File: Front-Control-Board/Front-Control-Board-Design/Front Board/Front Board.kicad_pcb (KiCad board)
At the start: 2 copper layers, 78 x 53.5 mm, 25 parts, among them J1 Conn_01x08, J2 Conn_01x23, Q1 2N7002, U1 MAX33054EASA+T, U2 TS2940CP33 ROG, U3 ESP32-DevKitC

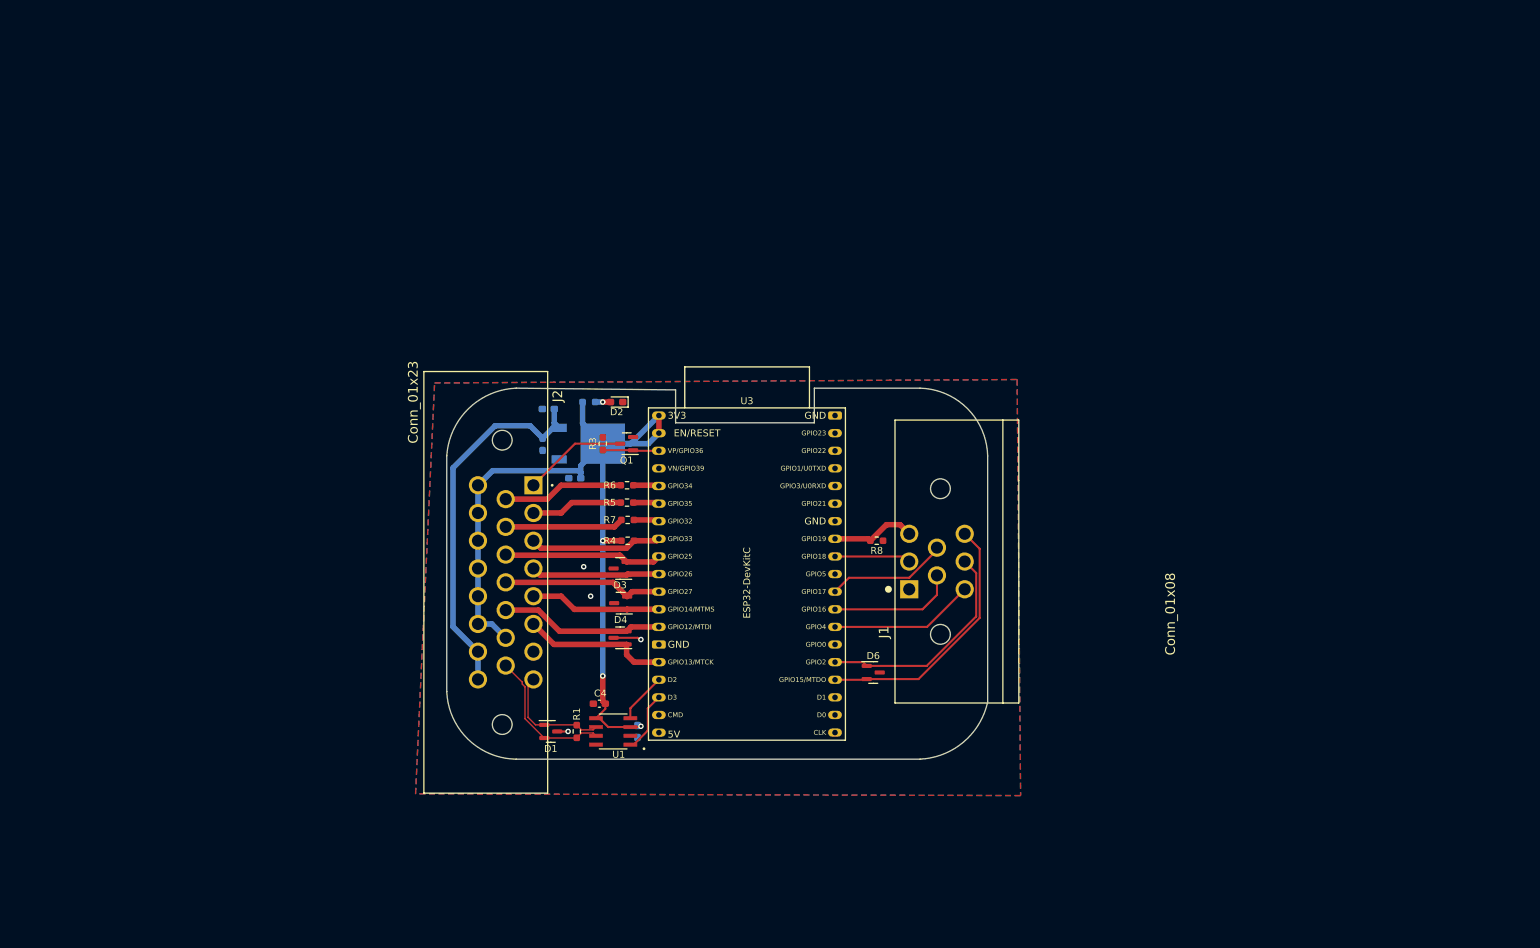
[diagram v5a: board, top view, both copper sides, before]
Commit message: pin layout updated needs PCB
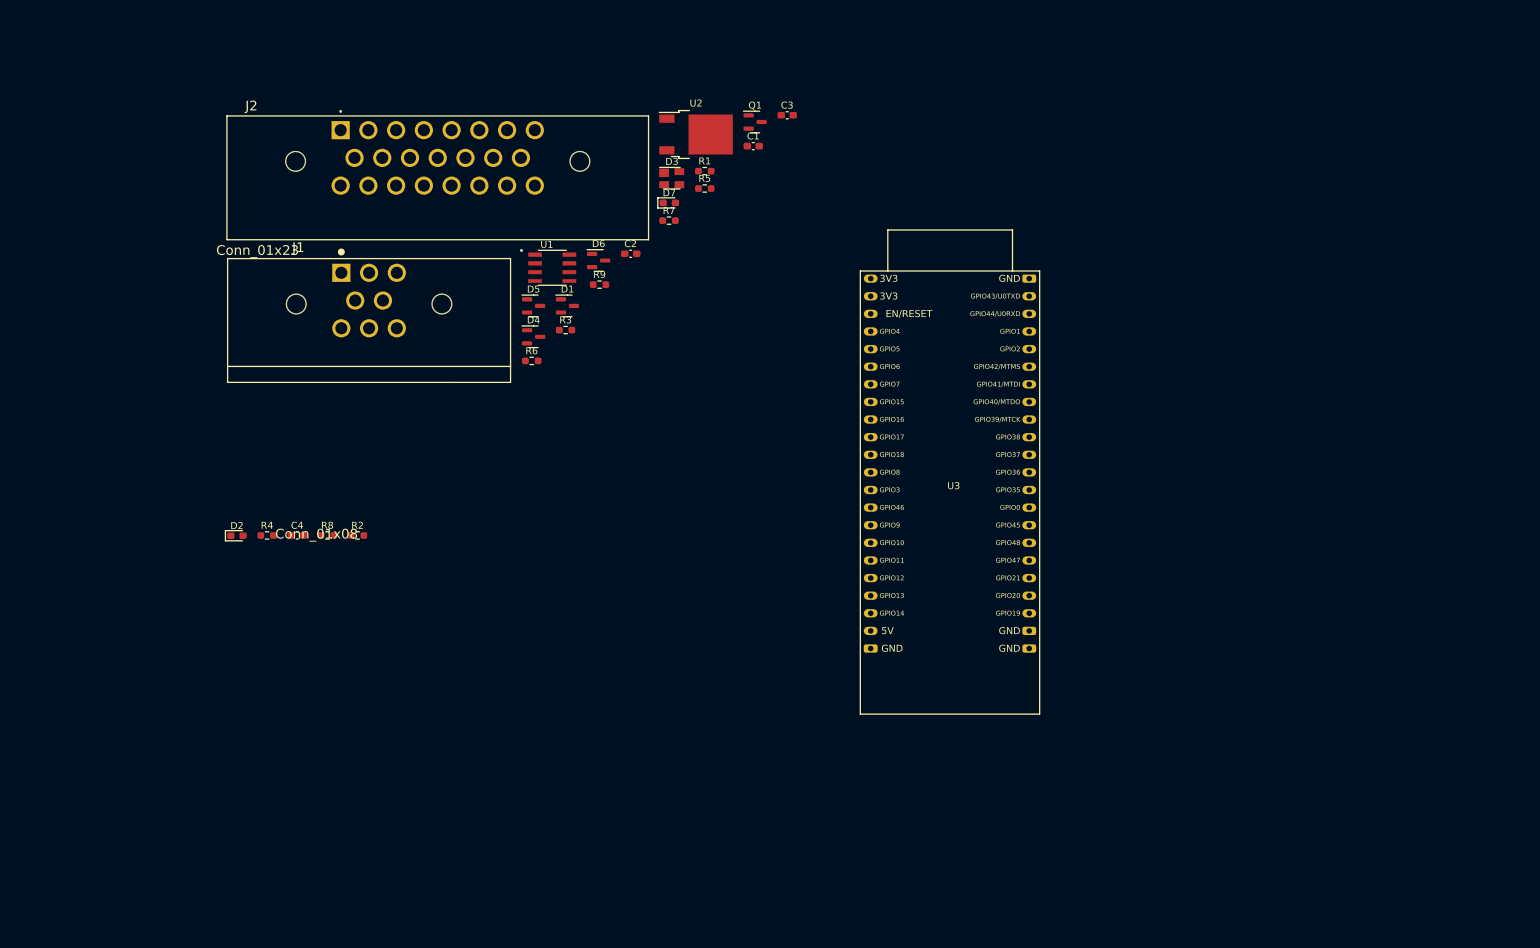
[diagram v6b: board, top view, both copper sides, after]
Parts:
- added R9: 100, Resistor_SMD:R_0603_1608Metric_Pad0.98x0.95mm_HandSolder, F.Cu at (132.0, 77.1)
- C1, C2, C3, D7, R2, U2: moved to F.Cu
- D3: value SP0502BAHT -> SP0503BAHT; footprint Package_TO_SOT_SMD:SOT-23 -> Package_TO_SOT_SMD:SOT-143
- R4: value 10k -> 100
- R7: value 100 -> 10k
- U3: footprint Espressif:ESP32-DevKitC -> AERO_Footprints:ESP32-DEV C
- moved C3 91.4 mm to (159.1, 52.6), turned to 0 degrees
- moved J1 90.4 mm to (98.8, 79.9), turned to 0 degrees
- moved R1 82.9 mm to (147.2, 60.7), turned to 0 degrees
- moved R8 79.2 mm to (92.8, 113.2), turned to 0 degrees
- moved D6 71.4 mm to (131.9, 73.6)
- moved U1 67.4 mm to (125.2, 74.6), turned to 0 degrees
- moved D1 61.4 mm to (127.4, 80.1)
- moved J2 58.3 mm to (94.7, 54.8), turned to 0 degrees
- moved D2 58.1 mm to (79.7, 113.3), turned to 0 degrees
- moved D3 56.8 mm to (142.4, 61.7), turned to 0 degrees
- moved R4 52.0 mm to (84.1, 113.2), turned to 0 degrees
- moved Q1 49.9 mm to (154.5, 53.6), turned to 0 degrees
- moved C4 49.9 mm to (88.4, 113.2), turned to 0 degrees
- moved D5 49.5 mm to (122.5, 80.1), turned to 0 degrees
- moved C1 48.1 mm to (154.2, 57.1), turned to 0 degrees
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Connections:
- D3 pad 1: /pedal_1 -> unconnected-(D3-Pad1)
- D3 pad 2: /stearing -> /R_wheel
- D3 pad 3: GND -> /L_wheel
- D4 pad 1: /R_wheel -> /R_sus
- D4 pad 2: /L_wheel -> /stearing
- D5 pad 1: /R_sus -> /pedal_0
- D5 pad 2: /L_sus -> /pedal_1
- D6 pad 1: /Brake_0 -> /Brake_1
- D6 pad 2: /Brake_1 -> /Brake_0
- R4 pad 1: /RTD_bttn -> Net-(U3-Pad35)
- R4 pad 2: VDD -> /AMS_Led
- R5 pad 1: Net-(R5-Pad1) -> /IMD_led
- R5 pad 2: /IMD_led -> Net-(U3-Pad34)
- R6 pad 1: Net-(R6-Pad1) -> Net-(U3-Pad33)
- R6 pad 2: /AMS_Led -> /RTD_led
- R7 pad 1: Net-(R7-Pad1) -> /RTD_bttn
- R7 pad 2: /RTD_led -> GND
- U1 pad 1: /CAN_TX -> /CAN_MOSI
- U1 pad 4: /CAN_RX -> /CAN_MISO
- U3 pad 10: /pedal_1 -> Net-(U3-Pad10)
- U3 pad 11: /L_wheel -> unconnected-(U3-Pad11)
- U3 pad 12: /R_wheel -> /LORA_SCK
- U3 pad 13: /L_sus -> /LORA_MISO
- U3 pad 15: /R_sus -> /Laura_MOSI
- U3 pad 16: /CAN_RX -> unconnected-(U3-Pad16)
- U3 pad 17: /CAN_TX -> unconnected-(U3-Pad17)
- U3 pad 23: /Brake_1 -> /LoRa_CS
- U3 pad 24: /Brake_0 -> unconnected-(U3-Pad24)
- U3 pad 25: unconnected-(U3-Pad25) -> /Brake_1
- U3 pad 26: /pedal_0 -> /Brake_0
- U3 pad 27: /LORA_RX -> /RTD_ind_sig
- U3 pad 28: /LORA_TX -> /RTD_bttn
- U3 pad 29: unconnected-(U3-Pad29) -> /CAN_CS
- U3 pad 3: /RTD_ind_sig -> /R_wheel
- U3 pad 30: /LORA NSS -> /CAN_SCK
- U3 pad 31: /LORA Reset -> /CAN_MISO
- U3 pad 33: unconnected-(U3-Pad33) -> Net-(U3-Pad33)
- U3 pad 34: unconnected-(U3-Pad34) -> Net-(U3-Pad34)
- U3 pad 35: unconnected-(U3-Pad35) -> Net-(U3-Pad35)
- U3 pad 36: unconnected-(U3-Pad36) -> /LORA Reset
- U3 pad 37: unconnected-(U3-Pad37) -> /CAN_MOSI
- U3 pad 4: unconnected-(U3-Pad4) -> /L_wheel
- U3 pad 5: Net-(R6-Pad1) -> /L_sus
- U3 pad 6: Net-(R5-Pad1) -> /R_sus
- U3 pad 7: Net-(R7-Pad1) -> /stearing
- U3 pad 8: /RTD_bttn -> /pedal_0
- U3 pad 9: /stearing -> /pedal_1
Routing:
- net VDD: track 125.7 -> 0.00 mm, vias 3 -> 0
- net +12V: track 54.2 -> 0.00 mm
- net /Brake_1: track 37.6 -> 0.00 mm
- net /Brake_0: track 32.1 -> 0.00 mm
- net /L_sus: track 23.6 -> 0.00 mm
- net /L_wheel: track 23.2 -> 0.00 mm
- net /stearing: track 22.8 -> 0.00 mm
- net /R_sus: track 21.2 -> 0.00 mm
- net /pedal_0: track 20.9 -> 0.00 mm
- net /CAN_P: track 20.7 -> 0.00 mm
- net /RTD_bttn: track 19.5 -> 0.00 mm
- net /R_wheel: track 18.9 -> 0.00 mm
- net /pedal_1: track 18.5 -> 0.00 mm
- net /LORA_RX: track 18.4 -> 0.00 mm
- net /LORA_TX: track 17.5 -> 0.00 mm
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- removed copper zone on B.Cu, net GND
- removed copper zone on F.Cu, net GND
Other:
- board outline removed

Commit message: Front board updated just needs traces
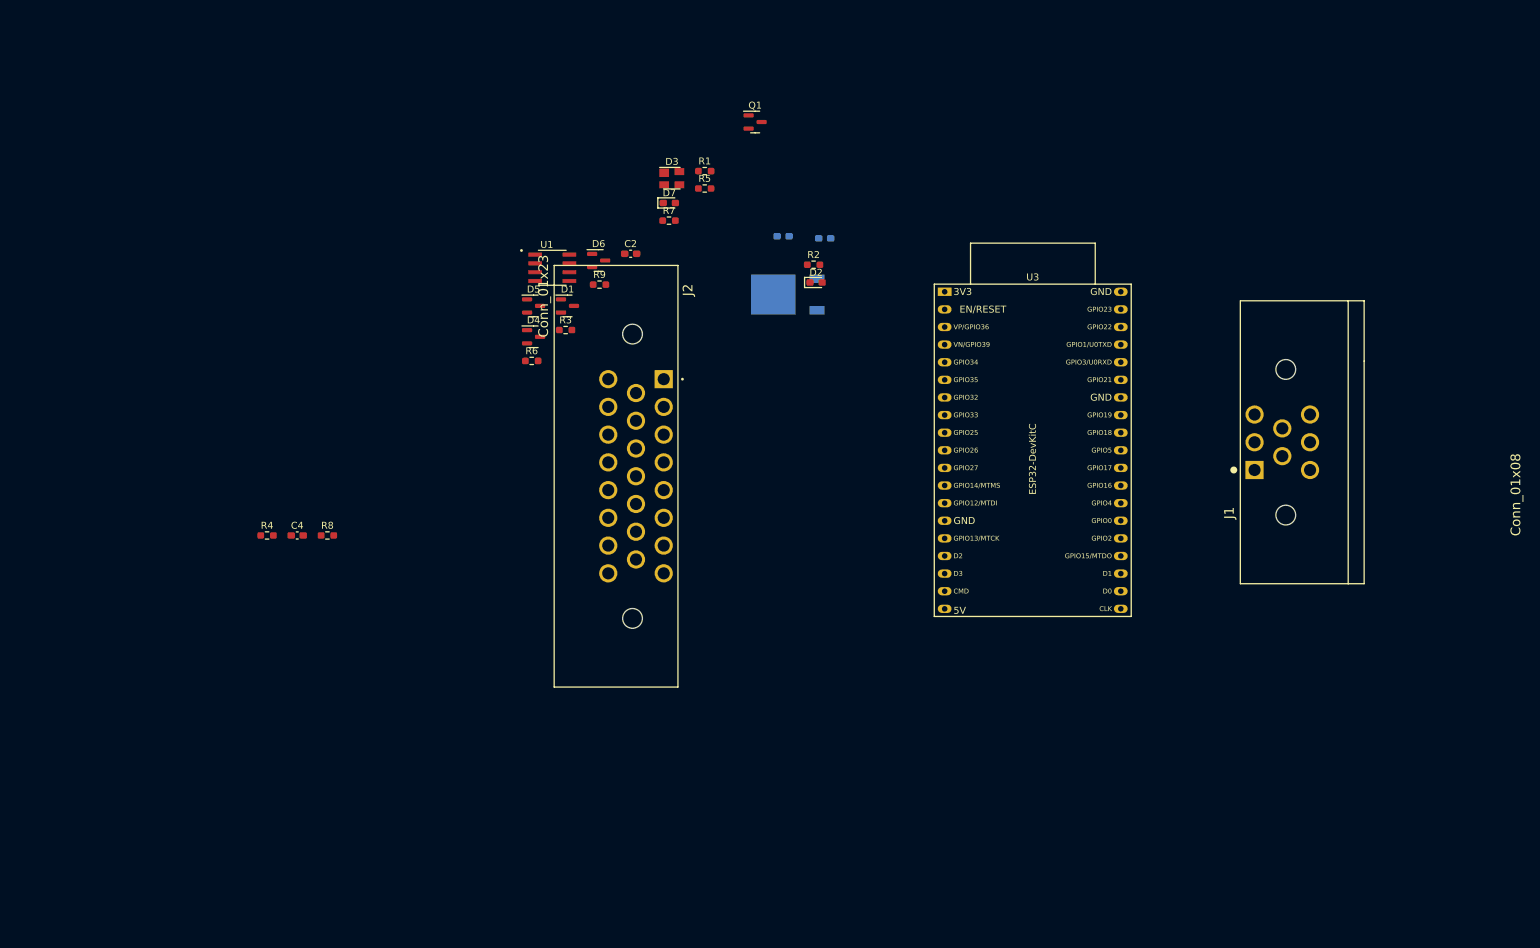
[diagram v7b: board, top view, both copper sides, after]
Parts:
- C1, C3, U2: moved to B.Cu
- U3: footprint AERO_Footprints:ESP32-DEV C -> esp32:ESP32-DevKitC
- moved J1 133.7 mm to (231.0, 99.8), turned to 90 degrees
- moved D2 91.2 mm to (163.3, 76.8)
- moved R2 76.5 mm to (162.9, 74.2)
- moved J2 58.8 mm to (141.3, 90.7), turned to -90 degrees
- moved U3 28.5 mm to (181.8, 78.1)
- moved U2 26.6 mm to (159.2, 78.5), turned to 180 degrees
- moved C3 18.6 mm to (164.5, 70.4), turned to 180 degrees
- moved C1 13.7 mm to (158.5, 70.1), turned to 180 degrees

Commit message: Front Board V1
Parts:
- added J3: Conn_01x08, AERO_Footprints:TE_1-776280-1_8pin_Horizontal, F.Cu at (166.7, 136.1)
- C2, C4, D1, D7, R1, R2, U1: moved to B.Cu
- J1: value Conn_01x08 -> Conn_01x14; footprint AERO_Footprints:TE_1-776280-1_8pin_Horizontal -> AERO_Footprints:TE_1-776266-1_14pin_Horizontal
- J2: value Conn_01x23 -> Conn_01x14; footprint AERO_Footprints:TE_1-770669-1_23pin_Horizontal -> AERO_Footprints:TE_1-776266-1_14pin_Horizontal
- moved R4 134.8 mm to (216.1, 85.9)
- moved R8 131.0 mm to (220.1, 82.3), turned to -90 degrees
- moved C4 126.6 mm to (211.7, 84.4), turned to 180 degrees
- moved D1 96.5 mm to (223.5, 88.5)
- moved R6 94.1 mm to (216.2, 93.6)
- moved D6 91.4 mm to (215.4, 110.8), turned to 180 degrees
- moved U1 90.2 mm to (214.4, 88.2)
- moved J2 88.6 mm to (229.3, 100.2), turned to 90 degrees
- moved R3 87.2 mm to (211.2, 106.9), turned to -90 degrees
- moved R7 84.8 mm to (219.4, 102.5), turned to 90 degrees
- moved Q1 80.8 mm to (215.5, 106.6)
- moved R1 77.6 mm to (219.7, 88.4), turned to 90 degrees
- moved R5 74.1 mm to (216.2, 90.1), turned to 180 degrees
- moved J1 71.7 mm to (159.3, 98.5), turned to -90 degrees
- moved C3 54.2 mm to (217.1, 83.3), turned to 90 degrees
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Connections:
- D1 pad 1: /CAN_N -> /CAN_P
- D1 pad 2: /CAN_P -> /CAN_N
- D3 pad 1: unconnected-(D3-Pad1) -> GND
- D3 pad 2: /R_wheel -> /L_sus
- D3 pad 4: /L_sus -> /R_wheel
- J1 pad 1: GND -> /R_wheel
- J1 pad 2: /LORA NSS -> /L_sus
- J1 pad 3: /LORA Reset -> /stearing
- J1 pad 4: /LORA_RX -> /WCB_status
- J1 pad 5: /LORA_TX -> /LORA_MISO
- J1 pad 6: /pedal_0 -> VDD
- J1 pad 7: /Brake_0 -> /R_sus
- J1 pad 8: /Brake_1 -> /pedal_1
- J2 pad 1: /RTD_ind_out -> /LoRa_CS
- J2 pad 10: /RTD_led -> unconnected-(J2-Pad10)
- J2 pad 11: /stearing -> /RTD_ind_out
- J2 pad 12: /L_wheel -> unconnected-(J2-Pad12)
- J2 pad 13: /L_sus -> /CAN_P
- J2 pad 14: VDD -> /CAN_N
- J2 pad 2: /IMD_led -> /Brake_0
- J2 pad 3: /RTD_bttn -> unconnected-(J2-Pad3)
- J2 pad 4: /pedal_1 -> /RTD_led
- J2 pad 5: /R_wheel -> /AMS_Led
- J2 pad 6: /R_sus -> /Brake_1
- J2 pad 7: unconnected-(J2-Pad7) -> /RTD_bttn
- J2 pad 8: /CAN_N -> /IMD_led
- J2 pad 9: /AMS_Led -> /LORA Reset
- U1 pad 8: GND -> /CAN_CS
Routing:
- net VDD: track 0.00 -> 154.8 mm
- net +12V: track 0.00 -> 72.3 mm
- net /L_wheel: track 0.00 -> 30.1 mm
- net /Laura_MOSI: track 0.00 -> 29.5 mm
- net /pedal_0: track 0.00 -> 29.0 mm
- net /CAN_MOSI: track 0.00 -> 28.1 mm
- net /LORA Reset: track 0.00 -> 27.8 mm
- net /Brake_1: track 0.00 -> 27.2 mm, vias 0 -> 1
- net /CAN_SCK: track 0.00 -> 26.9 mm
- net /R_sus: track 0.00 -> 24.9 mm
- net /Brake_0: track 0.00 -> 24.5 mm, vias 0 -> 1
- net /pedal_1: track 0.00 -> 23.9 mm
- net /LORA_SCK: track 0.00 -> 23.1 mm
- net /RTD_bttn: track 0.00 -> 22.7 mm
- net /CAN_N: track 0.00 -> 22.3 mm
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- added copper zone on B.Cu, net GND
- added copper zone on F.Cu, net GND
- added copper zone on B.Cu, net VDD
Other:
- board outline added: 85.2 x 70.7 mm
